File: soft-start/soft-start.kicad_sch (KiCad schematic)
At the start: 28 parts, among them M1 Motor_DC, Q1 IRFB3004PbF, SW1 L1's relay switch, U1 4011, U2 CD4060BE

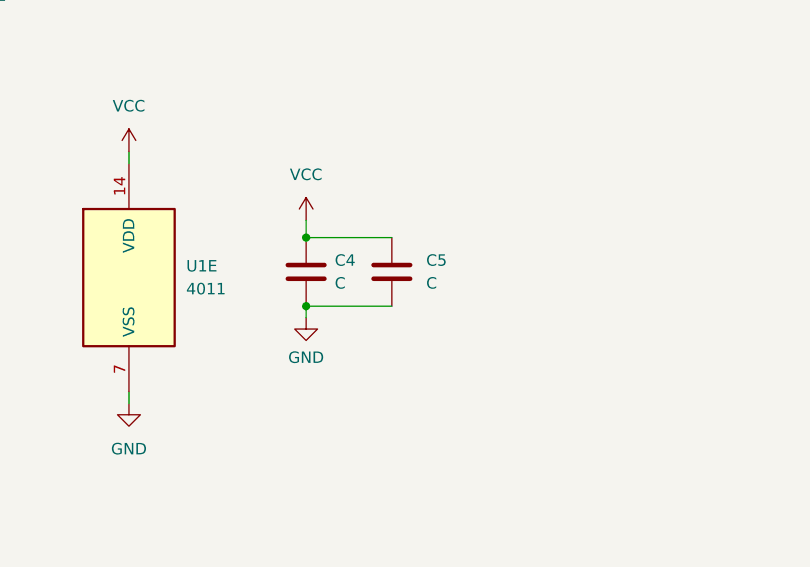
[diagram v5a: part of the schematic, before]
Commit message: [soft-start] Schematic - set values for C4 and C5
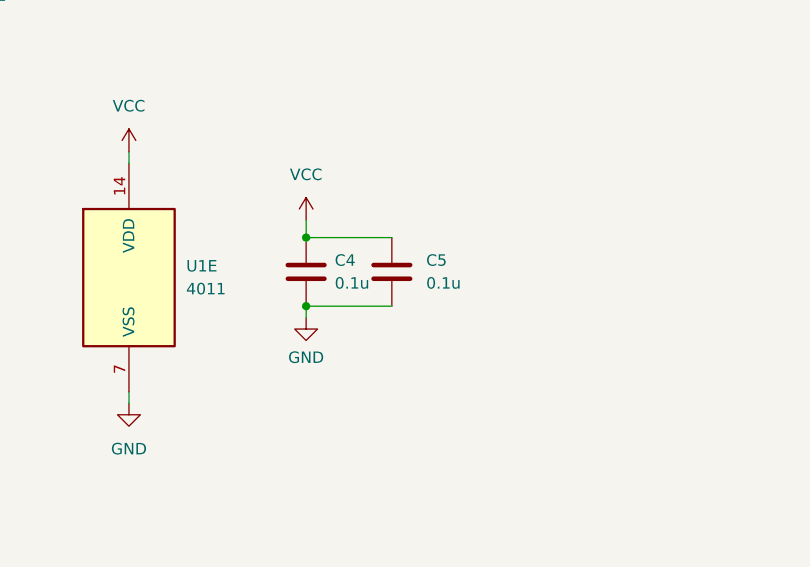
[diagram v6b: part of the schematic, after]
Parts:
- C4, C5: value C -> 0.1u
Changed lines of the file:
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@@
       (effects (font (size 1.27 1.27)) (justify left))
     )
-    (property "Value" "C" (at 270.51 132.715 0)
+    (property "Value" "0.1u" (at 270.51 132.715 0)
       (effects (font (size 1.27 1.27)) (justify left))
     )
@@
       (effects (font (size 1.27 1.27)) (justify left))
     )
-    (property "Value" "C" (at 260.35 132.715 0)
-      (effects (font (size 1.27 1.27)) (justify left))
-    )
+    (property "Value" "0.1u" (at 260.35 132.715 0)
+      (effects (font (size 1.27 1.27)) (justify left))
+    )

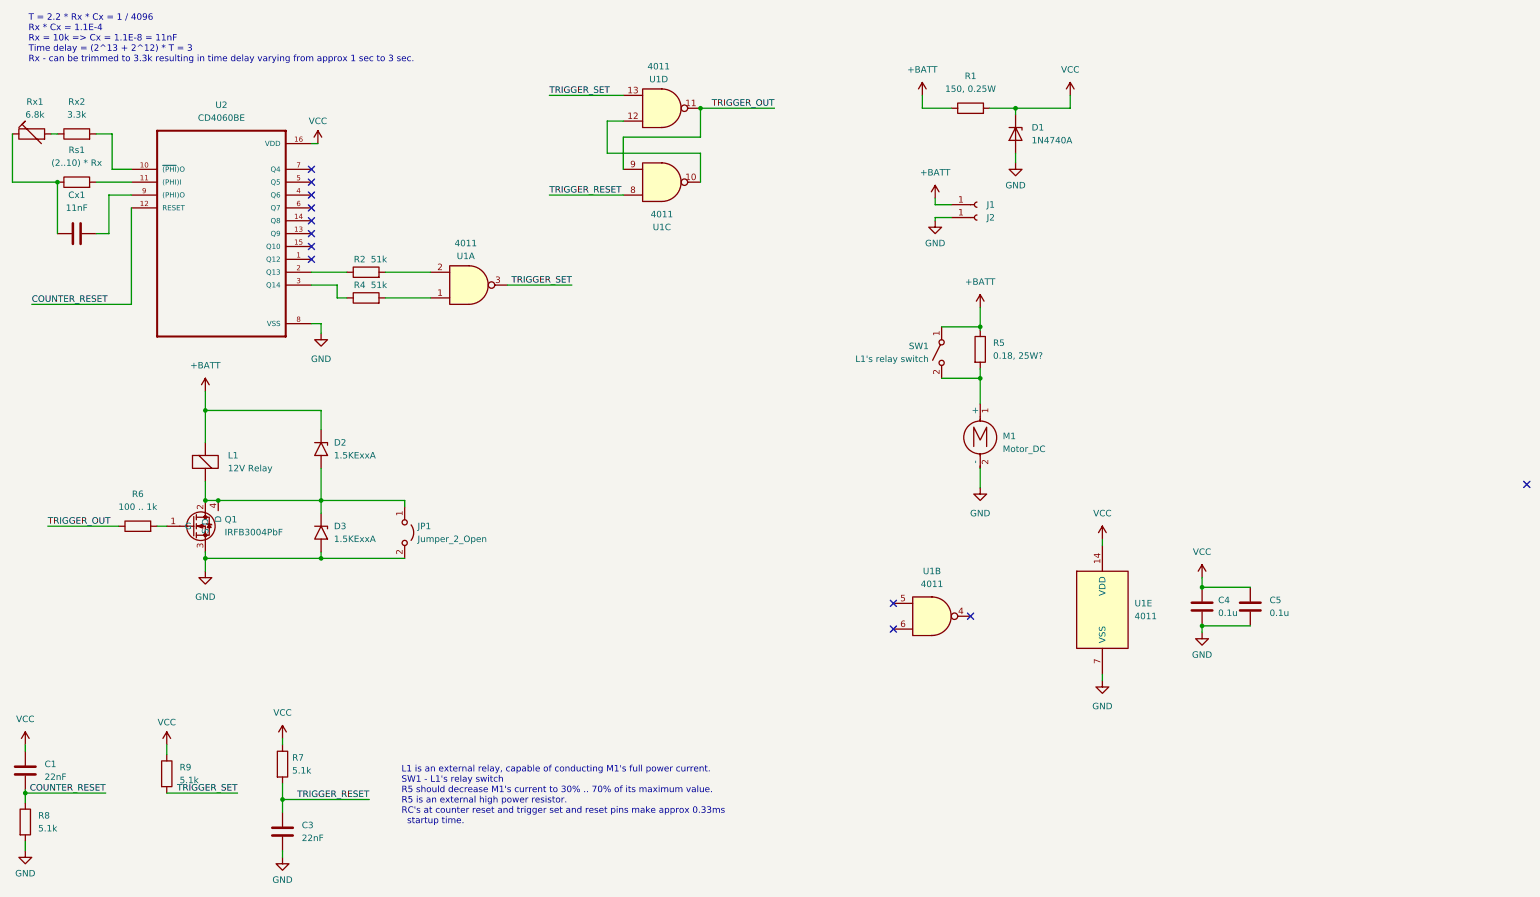
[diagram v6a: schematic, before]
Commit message: [soft-start] Schematic - add fixes for trigger. Update PCB.
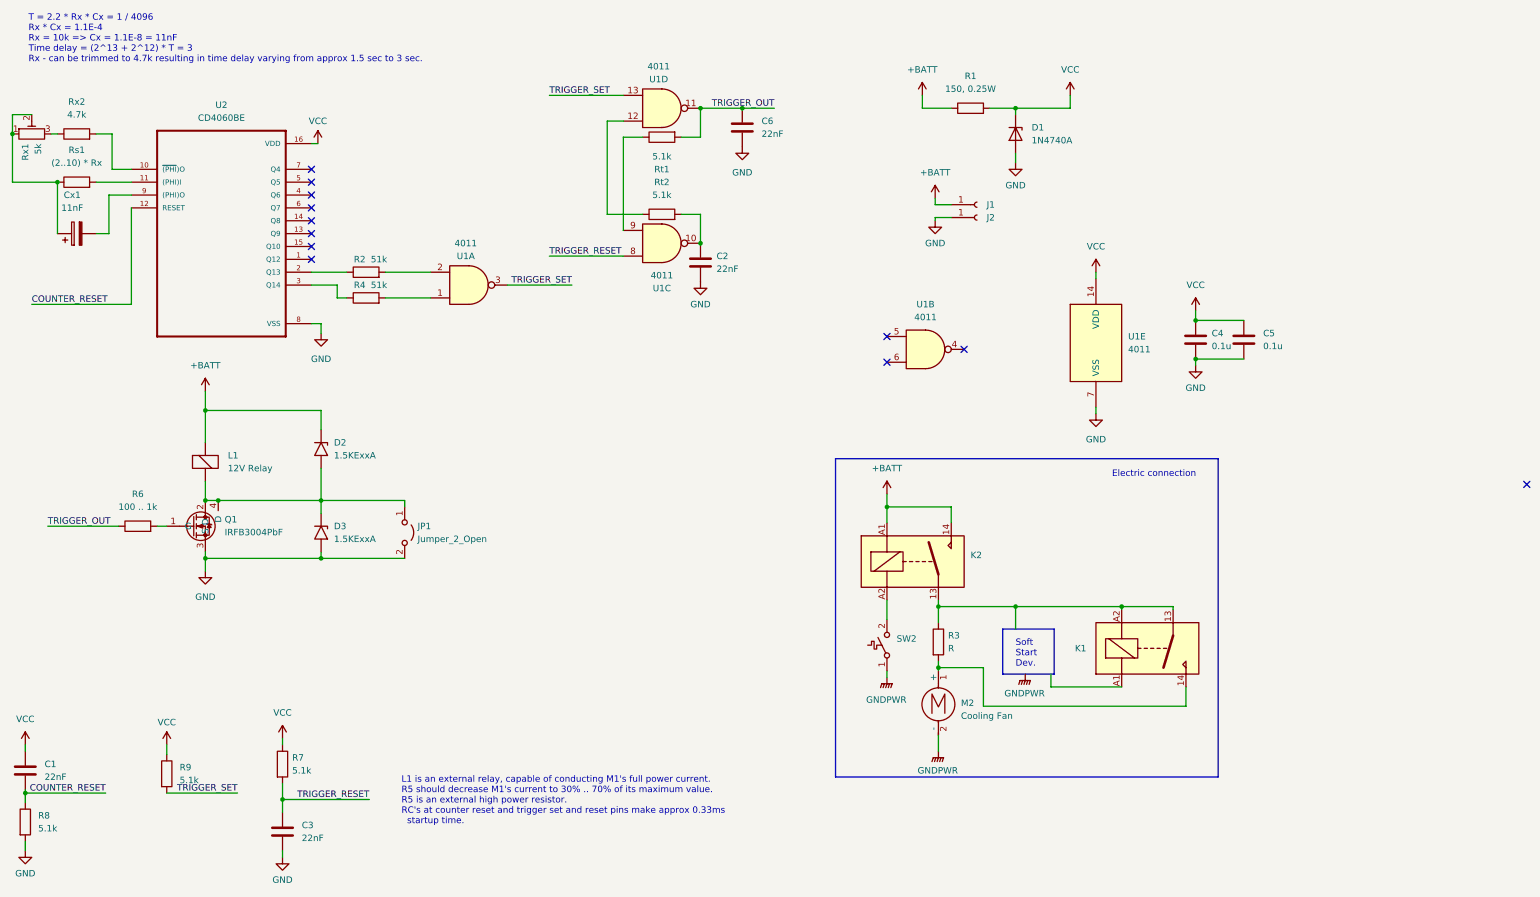
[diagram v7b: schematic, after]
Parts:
- removed Cx1: 11nF, Capacitor_THT:C_Disc_D6.0mm_W4.4mm_P5.00mm, symbol Device:C
- removed M1: Motor_DC, symbol Motor:Motor_DC
- removed R5: 0.18, 25W?, Connector_Wire:SolderWire-2.5sqmm_1x02_P7.2mm_D2.4mm_OD3.6mm, symbol Device:R
- removed Rx1: 6.8k, Resistor_THT:R_Axial_DIN0207_L6.3mm_D2.5mm_P7.62mm_Horizontal, symbol Device:R_Trim
- removed SW1: L1's relay switch, symbol Switch:SW_SPST
- added C2, C6: 22nF, Capacitor_THT:C_Disc_D6.0mm_W4.4mm_P5.00mm, symbol Device:C
- added Cx1: 11nF, Capacitor_THT:CP_Radial_D5.0mm_P2.50mm, symbol Device:C_Polarized
- added K1, K2: Relay_SPST-NO, symbol Relay:Relay_SPST-NO
- added M2: Cooling Fan, symbol Motor:Motor_DC
- added R3: R, symbol Device:R
- added Rt1, Rt2: 5.1k, Resistor_THT:R_Axial_DIN0204_L3.6mm_D1.6mm_P5.08mm_Horizontal, symbol Device:R
- added Rx1: 5k, Potentiometer_THT:Potentiometer_Bourns_3266W_Vertical, symbol Device:R_Potentiometer_Trim
- added SW2: SW_SPST_Temperature, symbol Switch:SW_SPST_Temperature
- Q1: footprint LIB:TO-220-3-4_Horizontal_TabDown -> Package_TO_SOT_SMD:TO-263-2
- R9: footprint Resistor_THT:R_Axial_DIN0207_L6.3mm_D2.5mm_P2.54mm_Vertical -> Resistor_THT:R_Axial_DIN0204_L3.6mm_D1.6mm_P5.08mm_Horizontal
- Rx2: value 3.3k -> 4.7k
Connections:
- net +BATT: now also K2.14, K2.A1
- net GND: now also C2.2, C6.2
- net TRIGGER_OUT: now also C6.1, Rt1.2; no longer U1.9
- net at U2.9 ((PHI)O): now also Cx1.2
- net at Rs1.1: now also Cx1.1, Rx1.1, Rx1.2
- net at U1.12: now also Rt2.1; no longer U1.10
- net at Rx2.1: now also Rx1.3
- new net: K2.A2, SW2.2 (B)
- new net: K1.13, K1.A2, K2.13, R3.1
- new net: K1.14, M2.1 (+), R3.2
- new net: Rt1.1, U1.9
- new net: C2.1, Rt2.2, U1.10
- new net GNDPWR: M2.2 (-), SW2.1 (A)
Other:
- note added: "Electric connection"
- note added: "L1 is an external relay, capable of conducting M1's full power current. R5 should decrease M1's current to 30% .. 70% of its maximum value. R5 is an external high power resistor. RC's at counter reset and trigger set and reset pins make approx 0.33ms startup time."
- note added: "Soft Start Dev."
- note added: "T = 2.2 * Rx * Cx = 1 / 4096 Rx * Cx = 1.1E-4 Rx = 10k => Cx = 1.1E-8 = 11nF Time delay = (2^13 + 2^12) * T = 3 Rx - can be trimmed to 4.7k resulting in time delay varying from approx 1.5 sec to 3 sec."
- note removed: "L1 is an external relay, capable of conducting M1's full power current. SW1 - L1's relay switch R5 should decrease M1's current to 30% .. 70% of its maximum value. R5 is an external high power resistor. RC's at counter reset and trigger set and reset pins make approx 0.33ms startup time."
- note removed: "T = 2.2 * Rx * Cx = 1 / 4096 Rx * Cx = 1.1E-4 Rx = 10k => Cx = 1.1E-8 = 11nF Time delay = (2^13 + 2^12) * T = 3 Rx - can be trimmed to 3.3k resulting in time delay varying from approx 1 sec to 3 sec."
- moved on the sheet: C4, C5, U1B, U1C, U1E

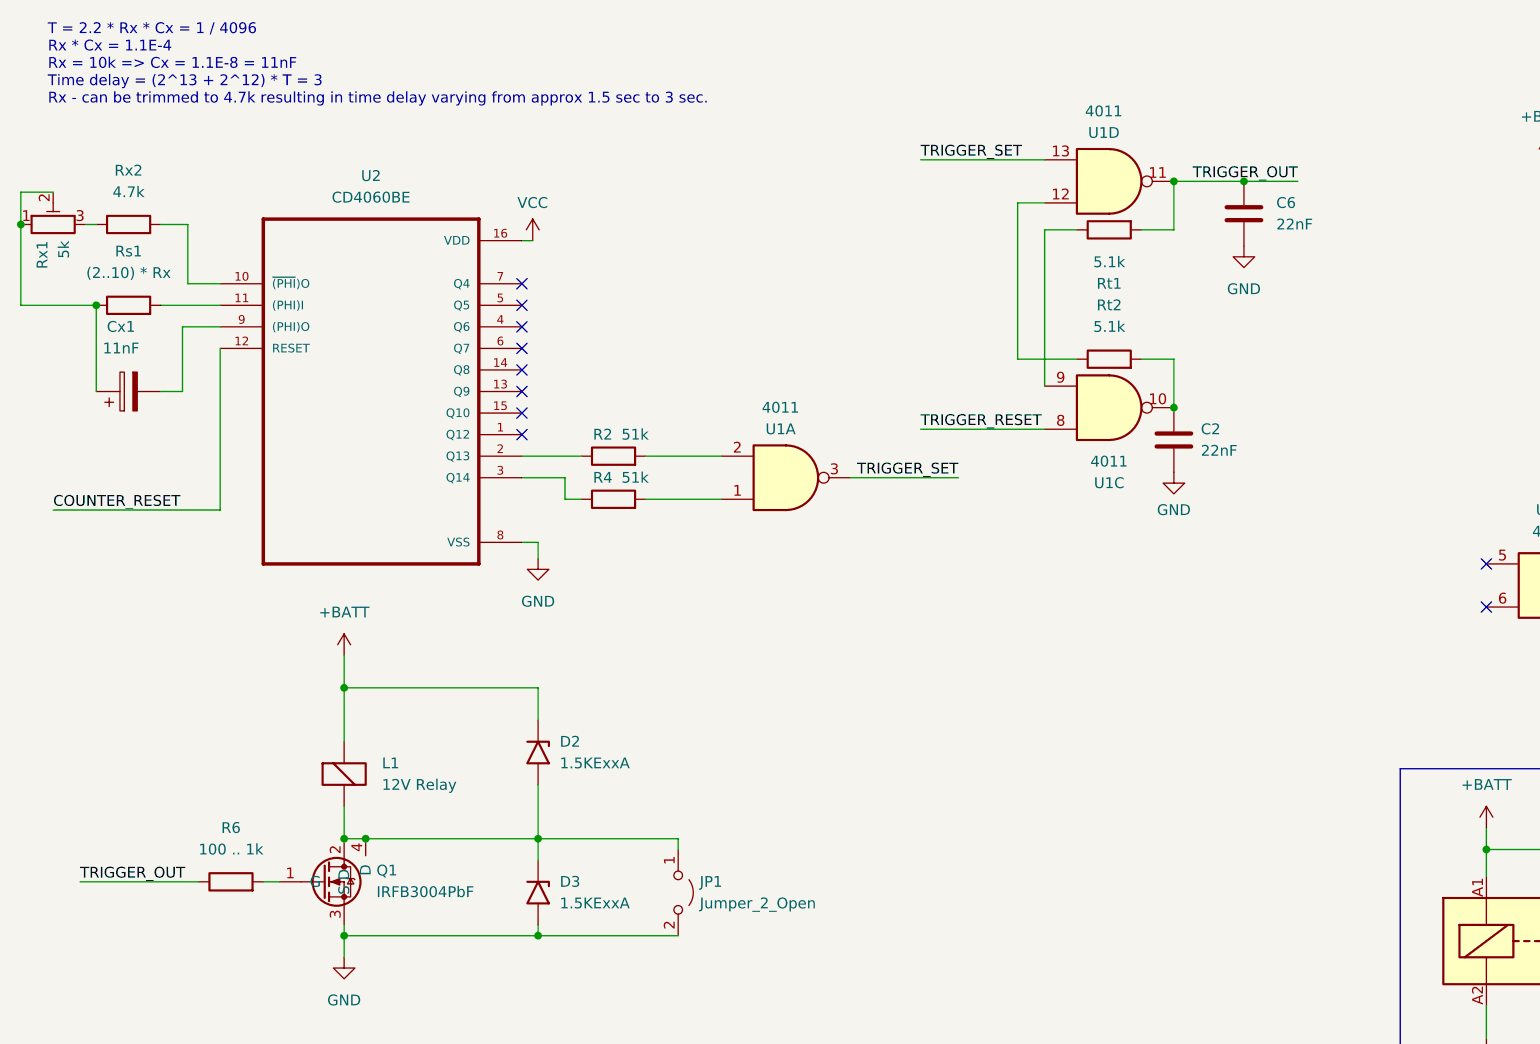
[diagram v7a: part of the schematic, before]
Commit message: [soft-start] Update values of timing RC
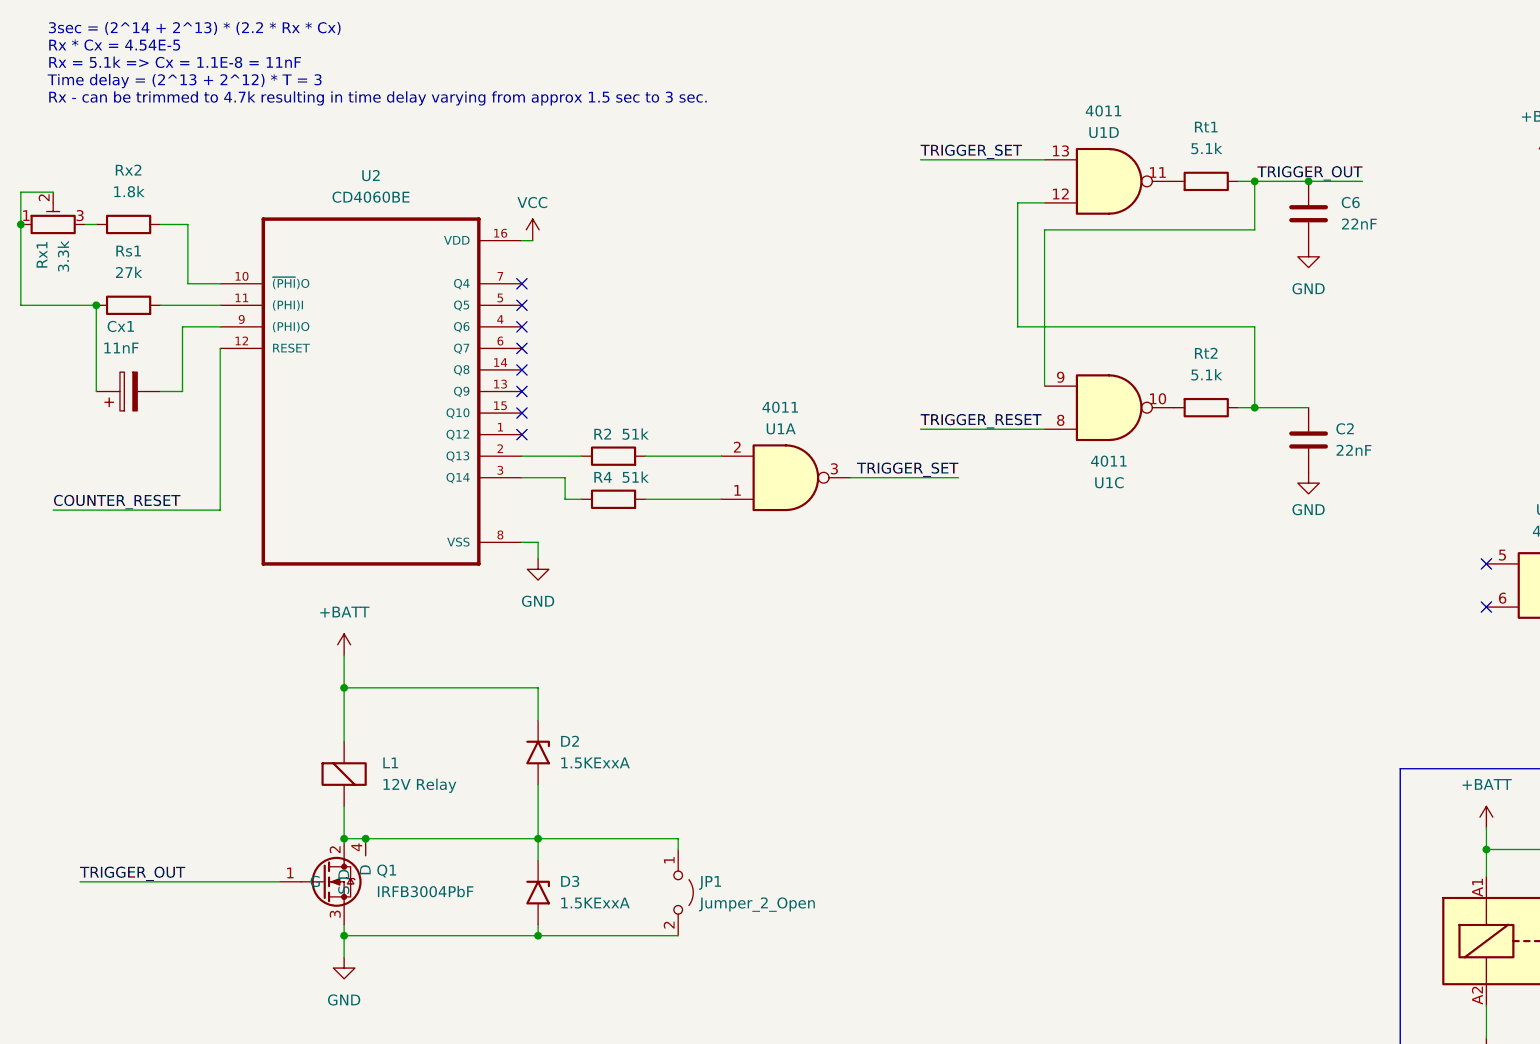
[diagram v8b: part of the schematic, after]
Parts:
- removed R6: 100 .. 1k, Resistor_THT:R_Axial_DIN0207_L6.3mm_D2.5mm_P2.54mm_Vertical, symbol Device:R
- Rs1: value (2..10) * Rx -> 27k
- Rx1: value 5k -> 3.3k
- Rx2: value 4.7k -> 1.8k
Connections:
- net TRIGGER_OUT: now also Q1.1 (G), Rt1.1, U1.9; no longer Rt1.2, U1.11
- net at Rt2.1, U1.12: now also C2.1
- net at Rt2.2, U1.10: no longer C2.1
- new net: Rt1.2, U1.11
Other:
- note added: "3sec = (2^14 + 2^13) * (2.2 * Rx * Cx) Rx * Cx = 4.54E-5 Rx = 5.1k => Cx = 1.1E-8 = 11nF Time delay = (2^13 + 2^12) * T = 3 Rx - can be trimmed to 4.7k resulting in time delay varying from approx 1.5 sec to 3 sec."
- note removed: "T = 2.2 * Rx * Cx = 1 / 4096 Rx * Cx = 1.1E-4 Rx = 10k => Cx = 1.1E-8 = 11nF Time delay = (2^13 + 2^12) * T = 3 Rx - can be trimmed to 4.7k resulting in time delay varying from approx 1.5 sec to 3 sec."
- moved on the sheet: C2, C6, Rt1, Rt2
